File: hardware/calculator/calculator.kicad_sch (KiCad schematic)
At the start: 15 parts, among them J1 USB_C_Receptacle_USB2.0_16P, SW1 RESET, SW2 BOOT, U1 ESP32-S3-WROOM-1, U2 TPD2EUSB30

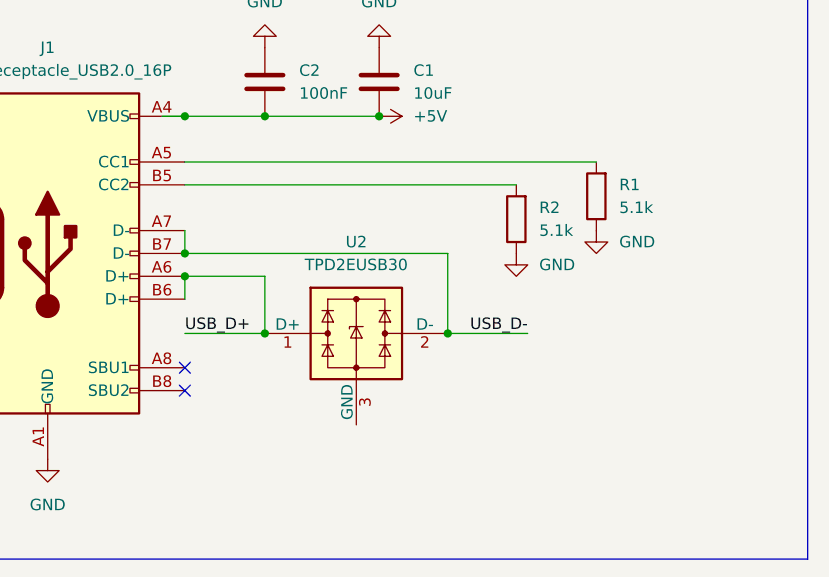
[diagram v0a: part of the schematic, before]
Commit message: Switched USB-C ESD IC
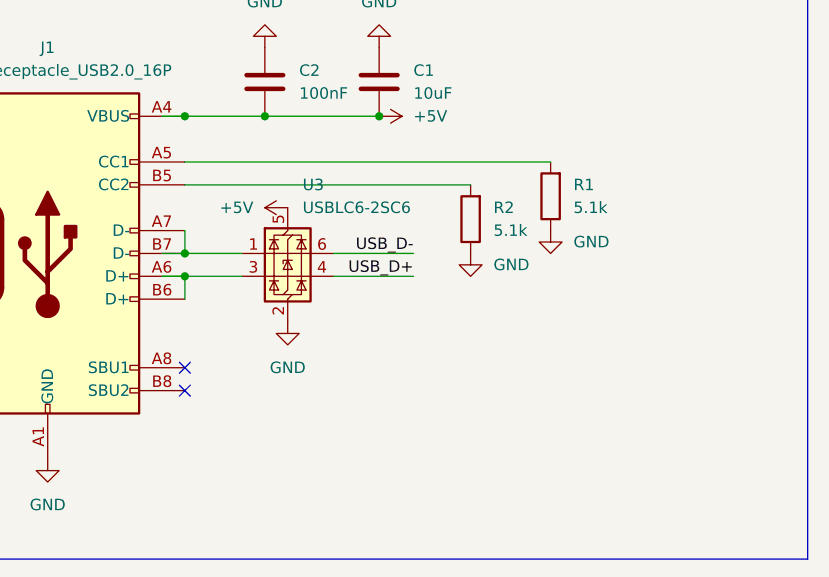
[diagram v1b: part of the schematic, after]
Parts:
- removed U2: TPD2EUSB30, Package_TO_SOT_SMD:Texas_DRT-3, symbol Power_Protection:TPD2EUSB30
- added U3: USBLC6-2SC6, Package_TO_SOT_SMD:SOT-23-6, symbol Power_Protection:USBLC6-2SC6
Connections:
- net +5V: now also U3.5 (VBUS)
- net GND: now also U3.2 (GND)
- net USB_D+: now also U3.4 (I/O2); no longer J1.A6 (D+), J1.B6 (D+)
- net USB_D-: now also U3.6 (I/O1); no longer J1.A7 (D-), J1.B7 (D-)
- new net: J1.A7 (D-), J1.B7 (D-), U3.1 (I/O1)
- new net: J1.A6 (D+), J1.B6 (D+), U3.3 (I/O2)
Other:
- moved on the sheet: R1, R2

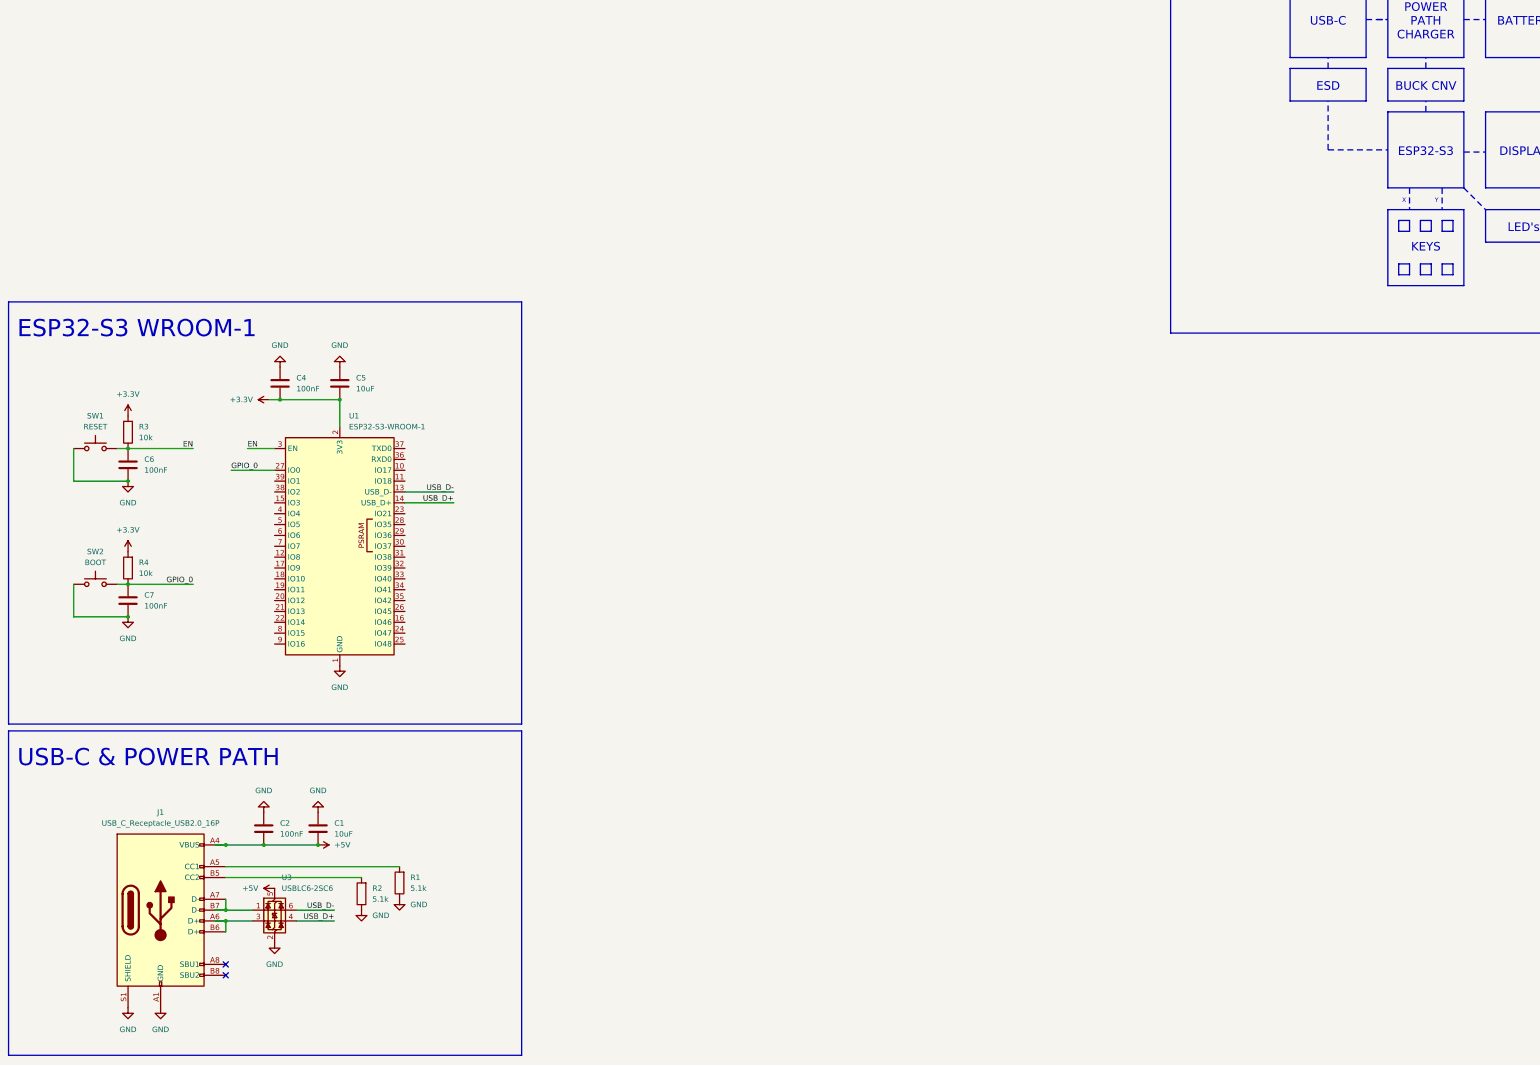
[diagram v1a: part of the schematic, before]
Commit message: Added Power Management
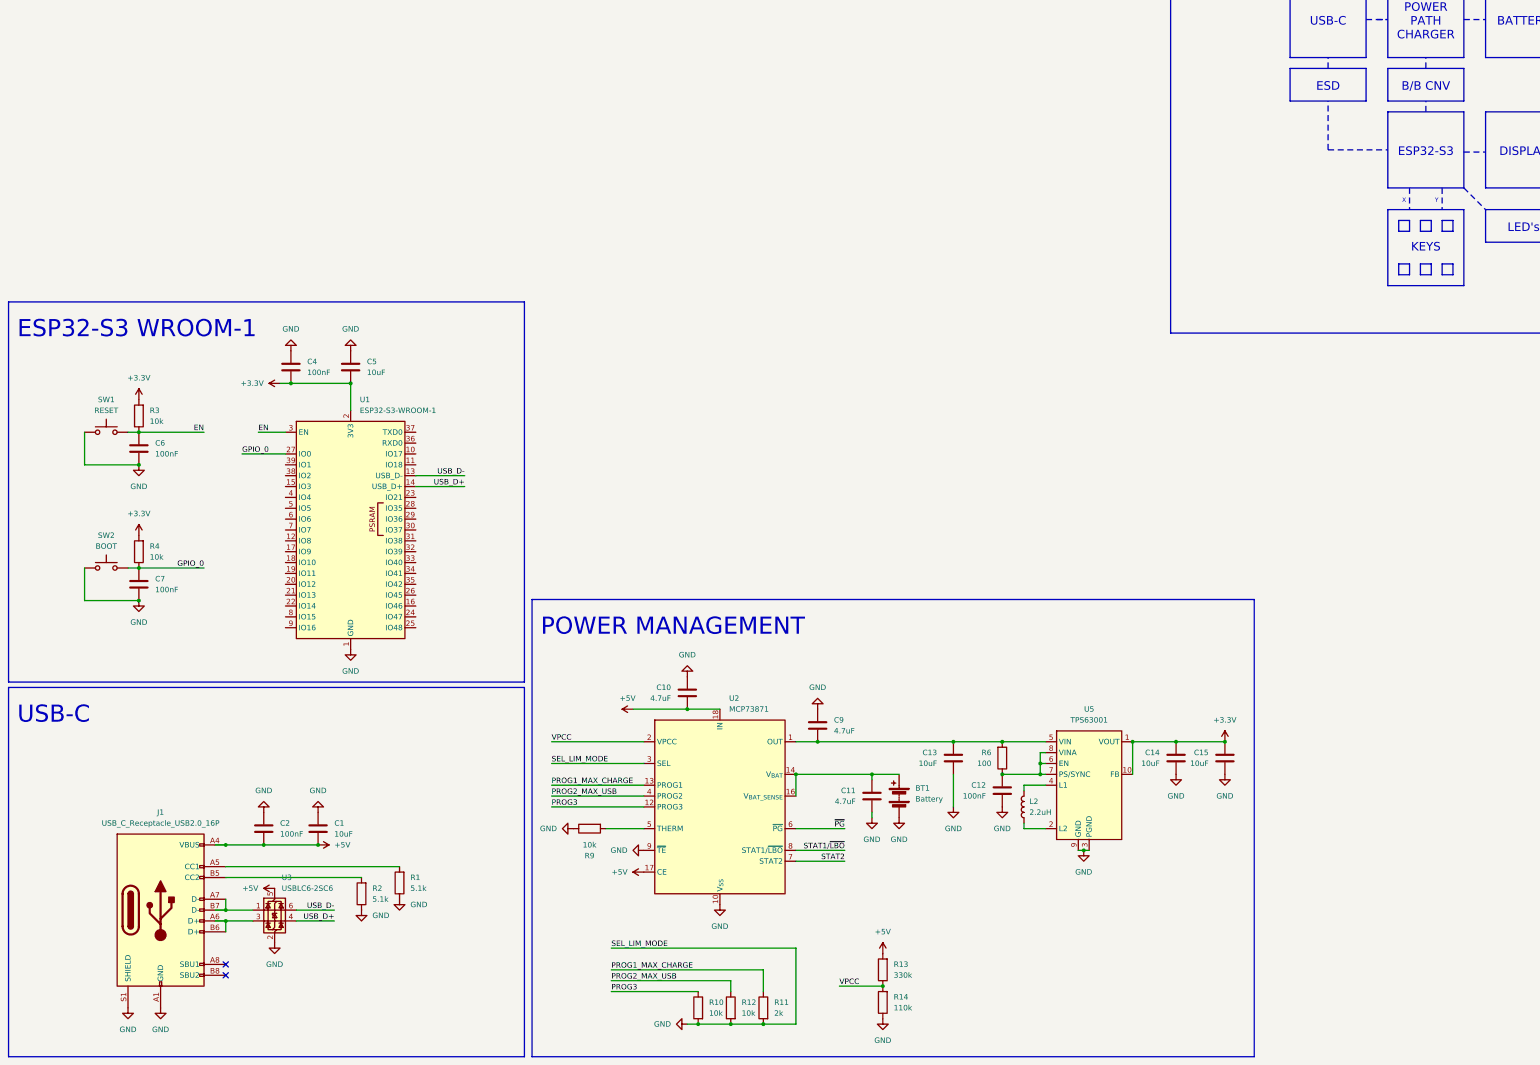
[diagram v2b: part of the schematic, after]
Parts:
- added BT1: Battery, symbol Device:Battery
- added C10, C11, C9: 4.7uF, symbol Device:C
- added C12: 100nF, symbol Device:C
- added C13, C14, C15: 10uF, symbol Device:C
- added L2: 2.2uH, symbol Device:L
- added R10, R12, R9: 10k, symbol Device:R
- added R11: 2k, symbol Device:R
- added R13: 330k, symbol Device:R
- added R14: 110k, symbol Device:R
- added R6: 100, symbol Device:R
- added U2: MCP73871, Package_DFN_QFN:QFN-20-1EP_4x4mm_P0.5mm_EP2.5x2.5mm, symbol Battery_Management:MCP73871
- added U5: TPS63001, Package_SON:Texas_DRC0010J_ThermalVias, symbol Regulator_Switching:TPS63001
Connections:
- net +3.3V: now also C14.1, C15.1, U5.1 (VOUT), U5.10 (FB)
- net +5V: now also C10.1, R13.2, U2.17 (CE), U2.18 (IN), U2.19 (IN)
- net GND: now also BT1.2 (-), C10.2, C11.2, C12.2, C13.2, C14.2, C15.2, C9.2, R10.2, R11.2, R12.2, R14.1, R9.1, U2.10 (V_{SS}), U2.11 (V_{SS}), U2.21 (V_{SS}), U2.3 (SEL), U2.9 (~{TE}), U5.11 (PGND), U5.3 (PGND), U5.9 (GND)
- new net: L2.1, U5.2 (L2)
- new net: L2.2, U5.4 (L1)
- new net: C13.1, C9.1, R6.2, U2.1 (OUT), U2.20 (OUT), U5.5 (VIN)
- new net: C12.1, R6.1, U5.6 (EN), U5.7 (PS/SYNC), U5.8 (VINA)
- new net: BT1.1 (+), C11.1, U2.14 (V_{BAT}), U2.15 (V_{BAT}), U2.16 (V_{BAT_SENSE})
- new net: R9.2, U2.5 (THERM)
- new net PROG1_MAX_CHARGE: R11.1, U2.13 (PROG1)
- new net PROG2_MAX_USB: R12.1, U2.4 (PROG2)
- new net PROG3: R10.1, U2.12 (PROG3)
- new net STAT1/~{LBO}: U2.8 (STAT1/~{LBO})
- new net STAT2: U2.7 (STAT2)
- new net VPCC: R13.1, R14.2, U2.2 (VPCC)
- new net ~{PG}: U2.6 (~{PG})
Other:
- note added: "B/B CNV"
- note added: "POWER MANAGEMENT"
- note removed: "BUCK CNV"
- note removed: "USB-C & POWER PATH"
- moved on the sheet: C4, C5, C6, C7, R3, R4, SW1, SW2, U1
